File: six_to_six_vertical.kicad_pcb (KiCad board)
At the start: 2 copper layers, 99.1 x 99.1 mm, 12 parts, among them J1 sma, J10 RF Conn, J11 RF Conn, J12 RF Conn, J2 sma, J3 sma, J4 sma, J5 sma, J6 sma, J7 RF Conn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

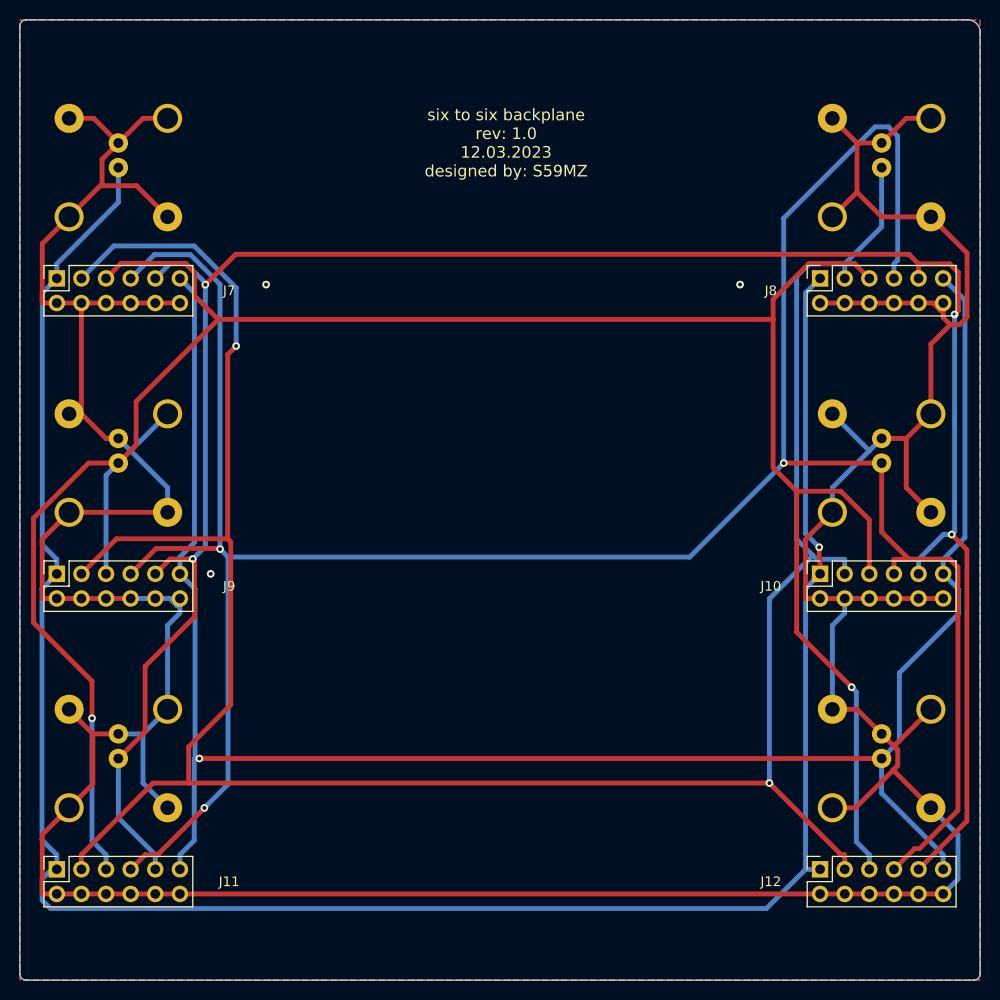
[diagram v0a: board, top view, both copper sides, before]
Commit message: renumber connectors
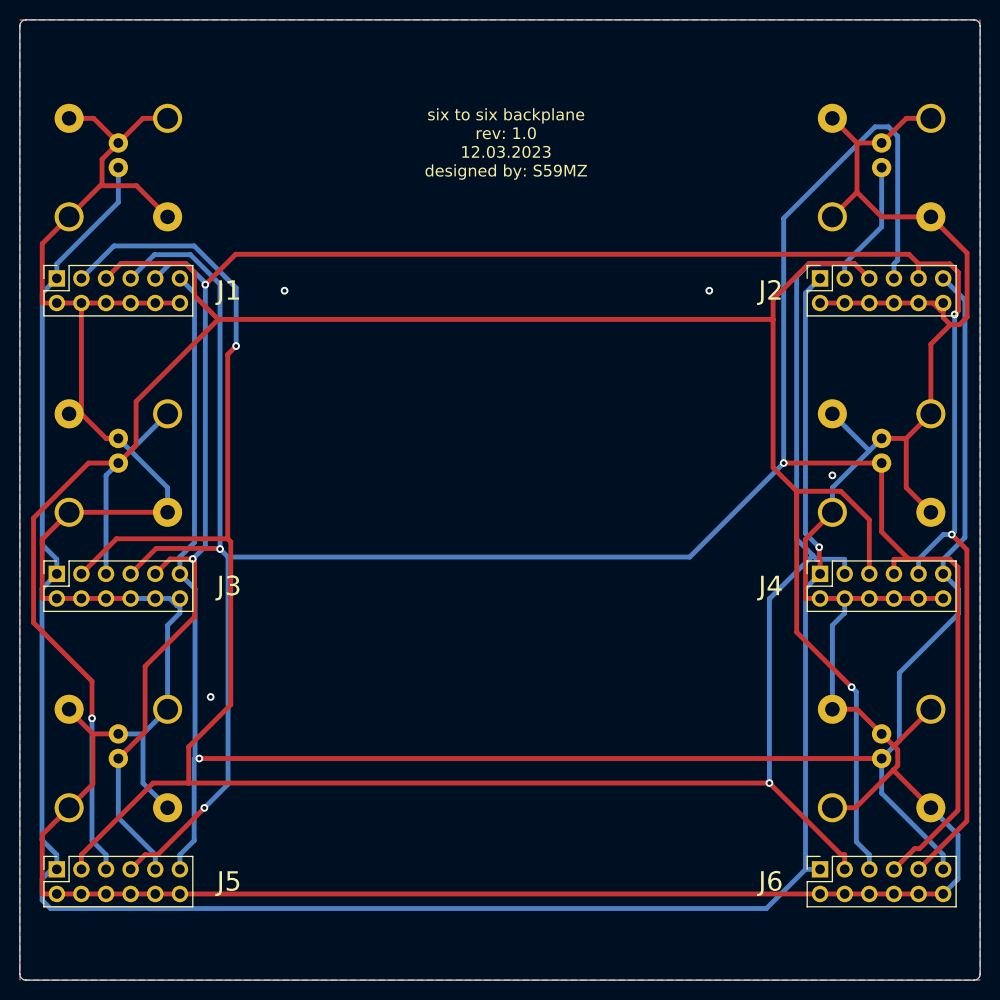
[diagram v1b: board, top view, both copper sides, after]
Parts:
- J10: renamed from J4; value sma -> bnc
- J11: renamed from J5; value sma -> bnc
- J12: renamed from J6; value sma -> bnc
- J7: renamed from J1; value sma -> bnc
- J8: renamed from J2; value sma -> bnc
- J9: renamed from J3; value sma -> bnc
- renumbered J7 to J1, J8 to J2, J9 to J3, J10 to J4, J11 to J5, J12 to J6
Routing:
- net GND: vias 3 -> 4
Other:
- outline, holes or cut-outs redrawn

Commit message: fixed RF board distances to fit on 30mm spacers
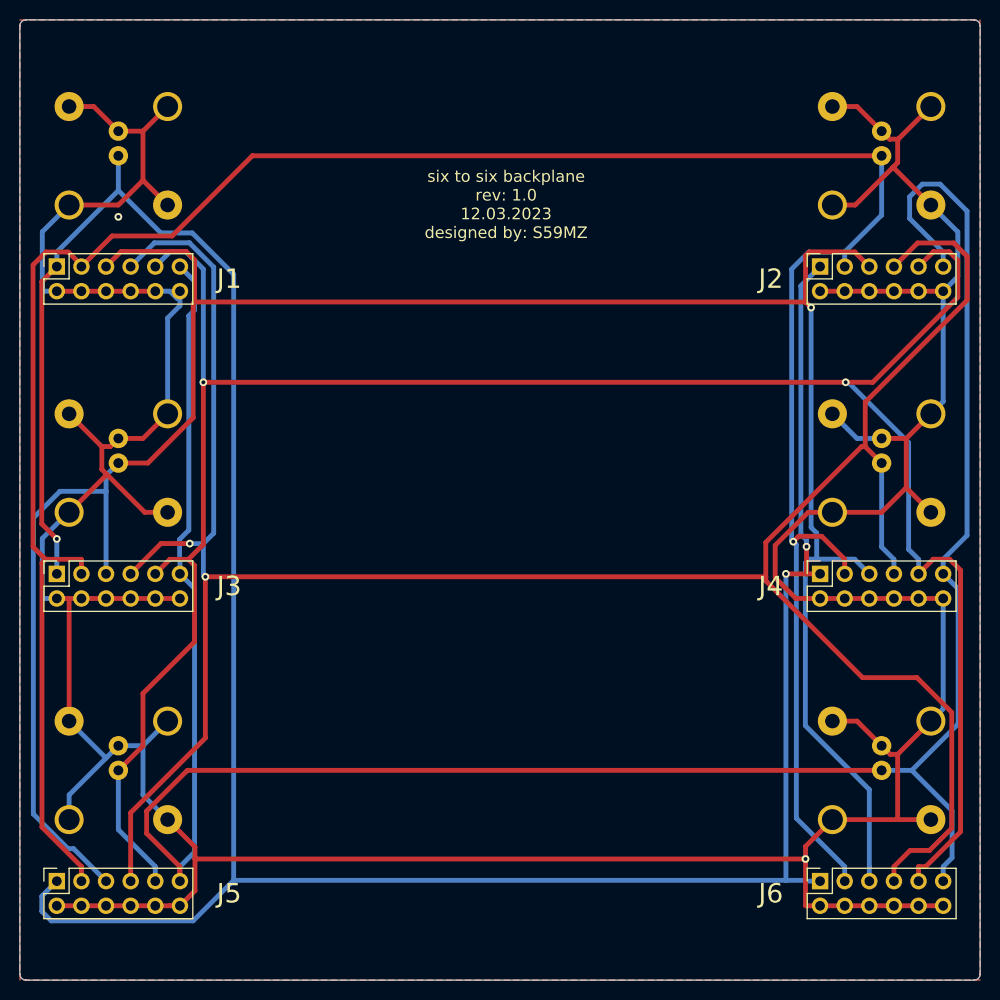
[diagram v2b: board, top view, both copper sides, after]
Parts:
- moved J1 1.22 mm to (101.6, 69.9)
- moved J11 1.22 mm to (108.0, 121.9)
- moved J12 1.22 mm to (186.7, 121.9)
- moved J2 1.22 mm to (180.3, 69.9)
- moved J5 1.22 mm to (101.6, 133.3)
- moved J6 1.22 mm to (180.3, 133.3)
- moved J7 1.22 mm to (108.0, 58.5)
- moved J8 1.22 mm to (186.7, 58.5)
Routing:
- net /rf-1: track 227.0 -> 279.2 mm, vias 1 -> 3
- net /rf-6: track 203.7 -> 246.4 mm, vias 1 -> 0
- net /rf-4: track 268.7 -> 255.9 mm, vias 3 -> 2
- net /rf-5: track 228.9 -> 232.3 mm, vias 4 -> 2
- net /rf-2: track 255.3 -> 257.3 mm, vias 2 -> 1
- net /rf-3: track 244.0 -> 242.7 mm, vias 2 -> 1
- net GND: vias 4 -> 2

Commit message: update board name
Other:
- board text added: "6 on 6 Backplane rev: 1.0 12.03.2023 S59MZ, S55O"
- board text removed: "six to six backplane rev: 1.0 12.03.2023 designed by: S59MZ"
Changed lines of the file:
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@@
   (gr_arc locked (start 196.85 142.875) (mid 196.664013 143.324013) (end 196.215 143.51) (layer "Edge.Cuts") (width 0.1))
   (gr_line locked (start 97.79 45.085) (end 97.79 142.875) (layer "Edge.Cuts") (width 0.1))
-  (gr_text "six to six backplane\nrev: 1.0\n12.03.2023\ndesigned by: S59MZ" (at 147.955 63.5) (layer "F.SilkS")
-    (effects (font (size 1.2 1.2) (thickness 0.15)))
+  (gr_text "6 on 6 Backplane\nrev: 1.0\n12.03.2023\nS59MZ, S55O" (at 148.59 64.77) (layer "F.SilkS")
+    (effects (font (size 1.3 1.3) (thickness 0.15)))
   )
   (segment (start 176.8176 101.6) (end 178.9422 101.6) (width 0.5) (layer "F.Cu") (net 1))
